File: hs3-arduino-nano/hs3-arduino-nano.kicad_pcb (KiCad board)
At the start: 2 copper layers, 17.8 x 43.2 mm, 40 parts, among them J1 PWR, J2 USB_B_Micro, J3 DBG, J4 I2C, J5 Sensors, J7 3V3, J8 GND, P3 CONN_01X01, P4 CONN_01X01, P5 CONN_01X01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

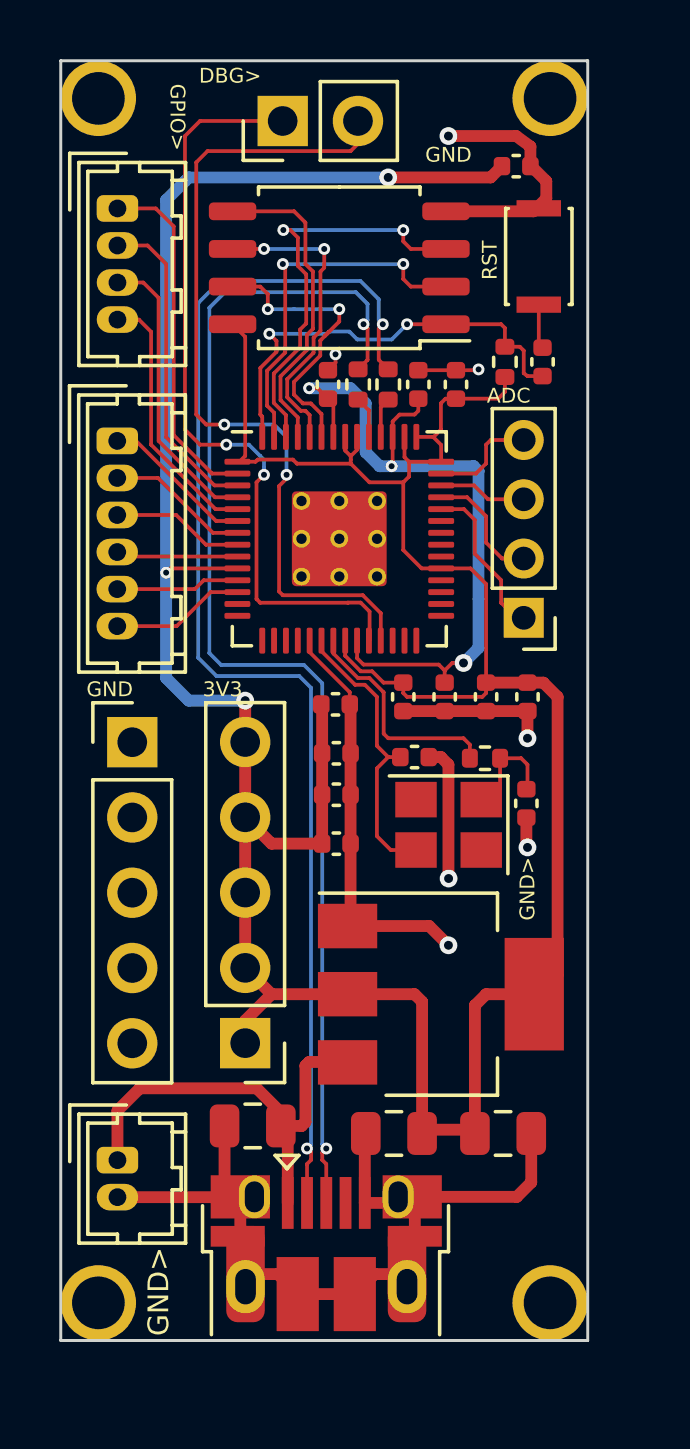
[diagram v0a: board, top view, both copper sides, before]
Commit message: Post-review place & route update pt. 1
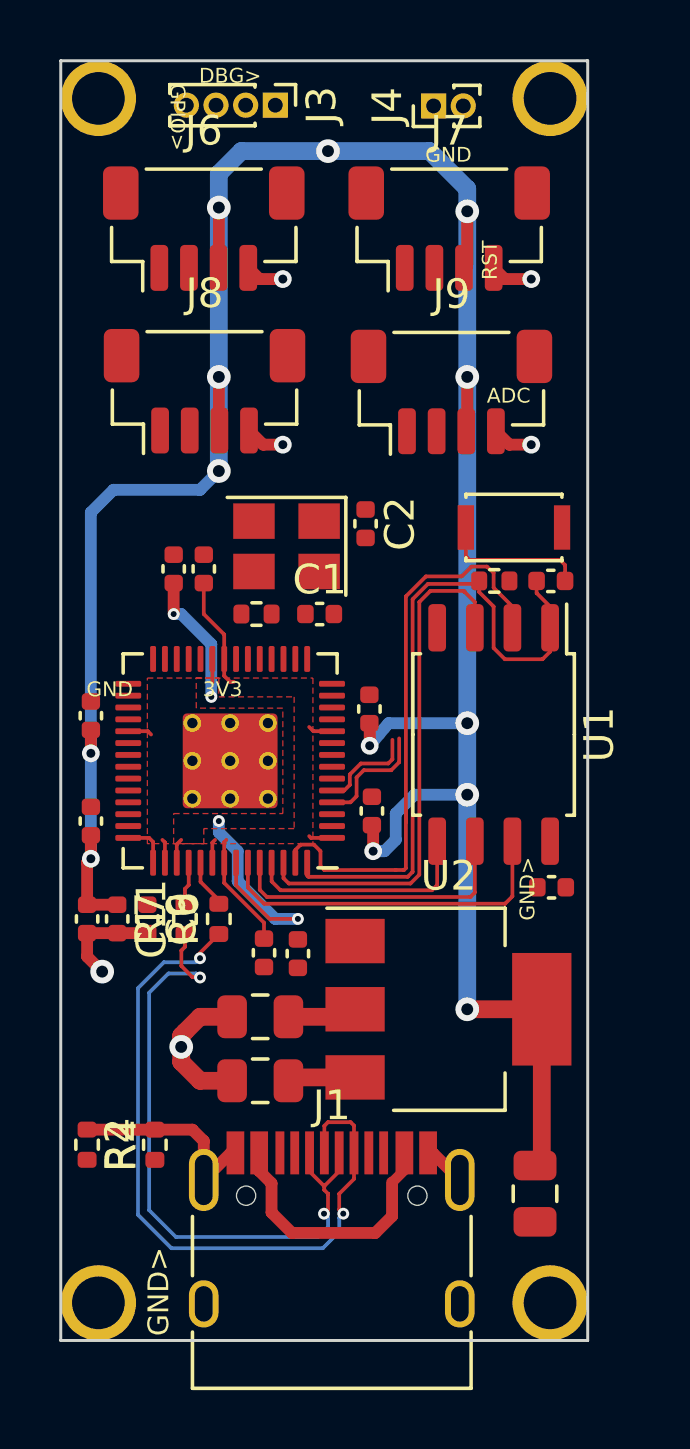
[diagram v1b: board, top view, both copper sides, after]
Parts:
- removed ADC: Conn_01x04, Connector_PinHeader_2.00mm:PinHeader_1x04_P2.00mm_Vertical
- removed J2: USB_B_Micro, RP2040:USB_Micro-B_Amphenol_10103594-0001LF_Horizontal_modified
- removed J5: Sensors, Connector_Hirose:Hirose_DF13-06P-1.25DSA_1x06_P1.25mm_Vertical
- added J6: CONN_01x04, Connector_JST:JST_SH_BM04B-SRSS-TB_1x04-1MP_P1.00mm_Vertical, F.Cu at (143.0, 73.1)
- added J9: CONN_01x04, Connector_JST:JST_SH_BM04B-SRSS-TB_1x04-1MP_P1.00mm_Vertical, F.Cu at (151.4, 78.6)
- added R6: 27, Resistor_SMD:R_0402_1005Metric, F.Cu at (143.5, 96.4)
- added R7: 27, Resistor_SMD:R_0402_1005Metric, F.Cu at (142.4, 96.4)
- J1: value PWR -> USB_C_Receptacle_USB2.0; footprint Connector_Hirose:Hirose_DF13-02P-1.25DSA_1x02_P1.25mm_Vertical -> Connector_USB:USB_C_Receptacle_HRO_TYPE-C-31-M-12
- J3: footprint Connector_PinHeader_2.54mm:PinHeader_1x02_P2.54mm_Vertical -> Connector_PinHeader_1.00mm:PinHeader_1x04_P1.00mm_Vertical
- J4: value I2C -> LED; footprint Connector_Hirose:Hirose_DF13-04P-1.25DSA_1x04_P1.25mm_Vertical -> Connector_PinHeader_1.00mm:PinHeader_1x02_P1.00mm_Vertical
- J7: value 3V3 -> CONN_01x04; footprint Connector_PinHeader_2.54mm:PinHeader_1x05_P2.54mm_Vertical -> Connector_JST:JST_SH_BM04B-SRSS-TB_1x04-1MP_P1.00mm_Vertical
- J8: value GND -> CONN_01x04; footprint Connector_PinHeader_2.54mm:PinHeader_1x05_P2.54mm_Vertical -> Connector_JST:JST_SH_BM04B-SRSS-TB_1x04-1MP_P1.00mm_Vertical
- R2: value 1k -> 5.1k
- R4: value 27 -> 5.1k
- R5: value 27 -> 1k
- U1: value NCP1117-3.3_SOT223 -> W25Q128JVS; footprint Package_TO_SOT_SMD:SOT-223-3_TabPin2 -> Package_SO:SOIC-8_5.23x5.23mm_P1.27mm
- U2: value W25Q128JVS -> NCP1117-3.3_SOT223; footprint Package_SO:SOIC-8_5.23x5.23mm_P1.27mm -> Package_TO_SOT_SMD:SOT-223-3_TabPin2
- moved J7 28.3 mm to (151.3, 73.1), turned to 0 degrees
- moved R4 27.2 mm to (139.1, 104.0)
- moved U2 25.3 mm to (151.3, 99.4), turned to 0 degrees
- moved C4 24.4 mm to (154.7, 95.3), turned to 180 degrees
- moved C11 21.4 mm to (140.1, 96.4), turned to -90 degrees
- moved C7 19.6 mm to (146.2, 97.6), turned to -90 degrees
- moved C9 19.0 mm to (141.1, 96.4), turned to -90 degrees
- moved R2 17.2 mm to (141.4, 104.0), turned to 90 degrees
- moved C17 15.4 mm to (139.1, 96.4)
- moved C16 12.4 mm to (145.0, 97.5)
- moved J8 12.1 mm to (143.0, 78.6)
- moved J4 11.2 mm to (150.8, 69.0), turned to 90 degrees
- moved C2 10.9 mm to (148.5, 83.1)
- moved XTAL1 10.9 mm to (145.8, 83.8)
- moved C13 10.3 mm to (143.0, 84.6), turned to 90 degrees
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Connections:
- J3 pad 1: /SWCLK -> +3V3
- J3 pad 2: /SWD -> /SWCLK
- J4 pad 1: /GPIO0 -> /GPIO2
- J4 pad 2: /GPIO1 -> /GPIO3
- J7 pad 1: +3V3 -> /GPIO17
- J7 pad 2: +3V3 -> /GPIO16
- J7 pad 4: +3V3 -> GND
- J8 pad 1: GND -> /GPIO17
- J8 pad 2: GND -> /GPIO16
- J8 pad 3: GND -> +3V3
- R2 pad 1: /XOUT -> Net-(J1-PadA5)
- R2 pad 2: Net-(C2-Pad1) -> GND
- R4 pad 1: /USB_D+ -> GND
- R4 pad 2: Net-(R4-Pad2) -> Net-(J1-PadB5)
- R5 pad 1: /USB_D- -> /XOUT
- R5 pad 2: Net-(R5-Pad2) -> Net-(C2-Pad1)
- U1 pad 1: GND -> /QSPI_SS
- U1 pad 2: +3V3 -> /QSPI_SD1
- U1 pad 3: VBUS -> /QSPI_SD2
- U2 pad 1: /QSPI_SS -> GND
- U2 pad 2: /QSPI_SD1 -> +3V3
- U2 pad 3: /QSPI_SD2 -> VBUS
- U3 pad 46: Net-(R5-Pad2) -> Net-(R7-Pad2)
- U3 pad 47: Net-(R4-Pad2) -> Net-(R6-Pad2)
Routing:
- net GND: track 61.5 -> 22.3 mm, vias 7 -> 6
- net /SWD: track 28.3 -> 0.00 mm, vias 2 -> 0
- net /SWCLK: track 26.3 -> 0.00 mm, vias 2 -> 0
- net /USB_D-: track 43.0 -> 20.8 mm
- net /USB_D+: track 41.8 -> 24.8 mm
- net /GPIO0: track 11.9 -> 0.00 mm
- net +3V3: track 120.4 -> 109.0 mm, vias 3 -> 13
- net /GPIO1: track 10.8 -> 0.00 mm
- net +1V1: track 24.6 -> 14.3 mm, vias 3 -> 4
- net /XIN: track 9.80 -> 0.00 mm
- net /QSPI_SS: track 14.9 -> 23.0 mm, vias 2 -> 0
- net /QSPI_SD1: track 12.3 -> 20.0 mm, vias 2 -> 0
- net /XOUT: track 7.59 -> 0.00 mm
- net /GPIO26_ADC0: track 6.29 -> 0.00 mm
- net /GPIO2: track 9.88 -> 4.00 mm
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- added copper zone on F.Cu, net +1V1
- added copper zone on F.Cu, net +3V3

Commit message: Post-review place & route update pt. 2
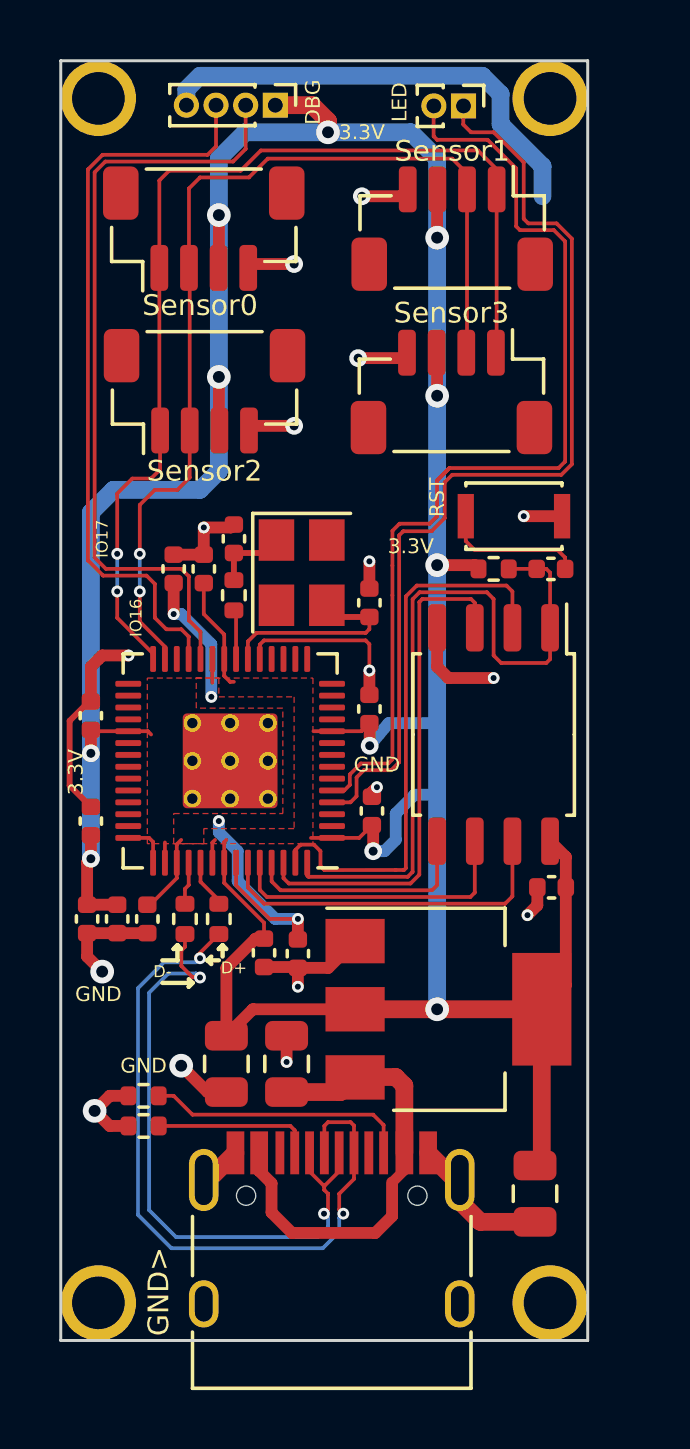
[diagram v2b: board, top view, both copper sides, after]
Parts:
- moved G2 12.8 mm to (147.1, 84.6)
- moved C2 4.47 mm to (144.0, 83.6), turned to 90 degrees
- moved R4 2.52 mm to (141.0, 102.4), turned to 0 degrees
- moved C6 1.96 mm to (143.8, 101.3), turned to -90 degrees
- moved C1 1.72 mm to (148.6, 85.7), turned to 90 degrees
- moved C3 1.06 mm to (145.8, 101.3), turned to 90 degrees
- moved XTAL1 1.02 mm to (146.3, 84.7), turned to -90 degrees
- moved J4 1.01 mm to (151.8, 69.0), turned to -90 degrees
- moved R5 0.99 mm to (144.0, 85.5), turned to 90 degrees
- moved R2 0.74 mm to (141.0, 103.4), turned to 180 degrees
- moved R3 0.41 mm to (152.8, 84.6), turned to 0 degrees
- moved R1 0.41 mm to (154.7, 84.6)
- moved SW1 0.38 mm to (153.5, 82.8)
- moved Sensor1 0.10 mm to (151.4, 73.1), turned to 180 degrees
- turned Sensor3 to 180 degrees
- renumbered J7 to Sensor1, J8 to Sensor2, J9 to Sensor3
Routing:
- net GND: track 22.3 -> 64.6 mm, vias 6 -> 17
- net /GPIO17: track 0.00 -> 35.9 mm, vias 0 -> 2
- net /GPIO16: track 0.00 -> 33.4 mm, vias 0 -> 2
- net /GPIO3: track 3.34 -> 33.9 mm
- net /GPIO2: track 4.00 -> 33.0 mm
- net /SWCLK: track 0.00 -> 26.3 mm
- net /SWD: track 0.00 -> 25.1 mm
- net +3V3: track 109.0 -> 130.1 mm, vias 13 -> 11
- net Net-(J1-PadB5): track 0.00 -> 8.94 mm
- net /XIN: track 0.00 -> 6.87 mm
- net Net-(J1-PadA5): track 0.00 -> 5.41 mm
- net VBUS: track 11.6 -> 15.7 mm
- net +1V1: track 14.3 -> 16.9 mm
- net Net-(C2-Pad1): track 0.00 -> 2.53 mm
- net /XOUT: track 0.00 -> 1.67 mm
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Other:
- board text added: "3.3V"
- board text added: "D+"
- board text added: "D-"
- board text added: "DBG"
- board text added: "IO16"
- board text added: "IO17"
- board text added: "LED"
- board text removed: "3V3"
- board text removed: "ADC"
- board text removed: "ADC0"
- board text removed: "ADC1"
- board text removed: "ADC2"
- board text removed: "ADC3"
- board text removed: "DBG>"
- board text removed: "GPIO>"
- board text removed: "IO0"
- board text removed: "IO1"
- board text removed: "IO2"
- board text removed: "IO3"
- board text removed: "IO4"
- board text removed: "IO5"
- board text removed: "IO6"
- board text removed: "IO7"
- board text removed: "IO8"
- board text removed: "IO9"

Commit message: Shortening traces around 3.3V pins
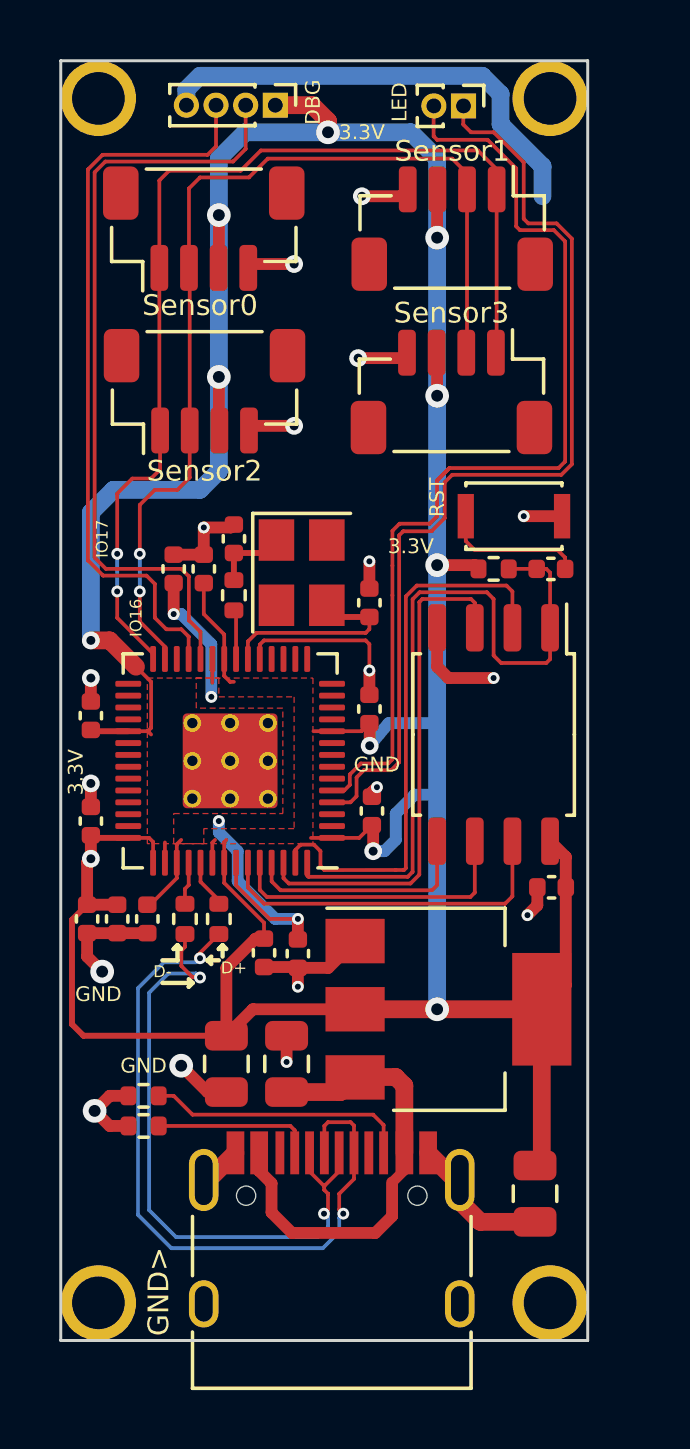
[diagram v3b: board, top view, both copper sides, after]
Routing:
- net +3V3: track 130.1 -> 137.2 mm
- net GND: track 64.6 -> 59.4 mm, vias 17 -> 18

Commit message: Minor cleanup in PCB, adding part numbers to BOM
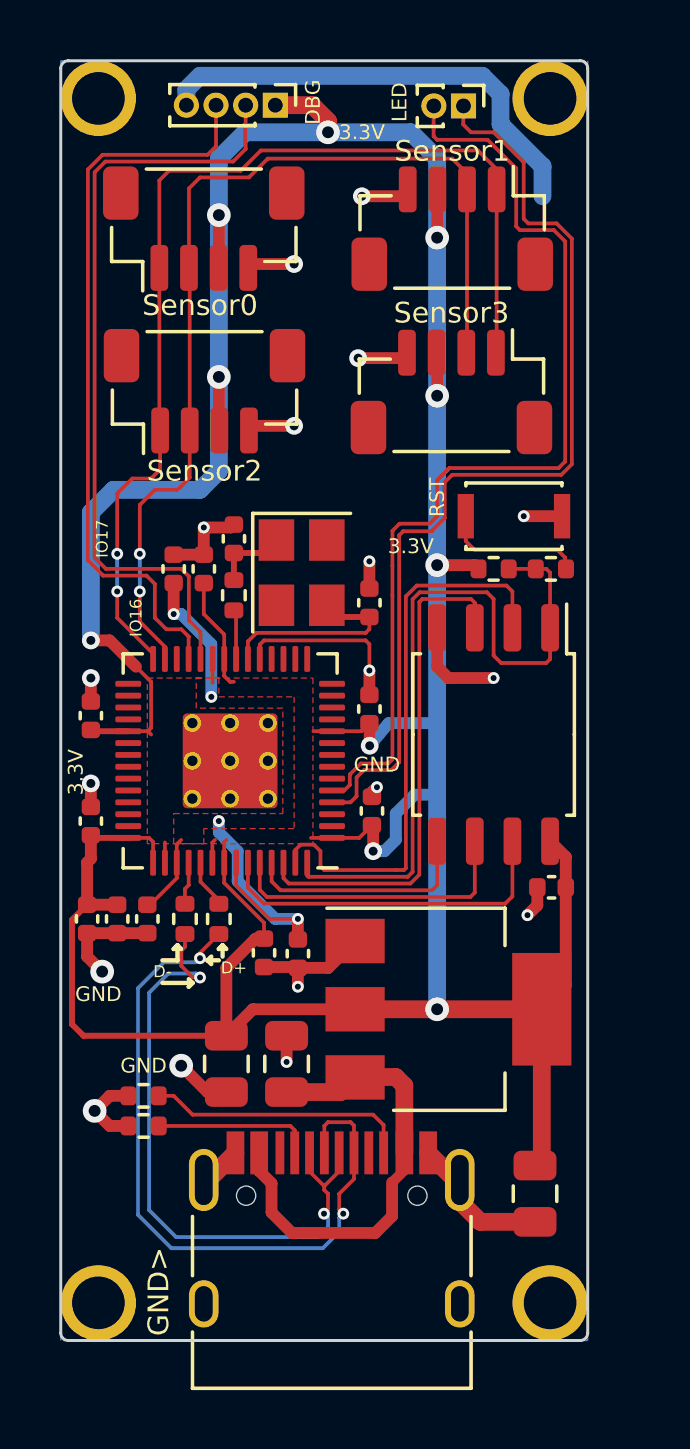
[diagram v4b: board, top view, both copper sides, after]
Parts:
- R1: footprint Capacitor_SMD:C_0402_1005Metric -> Resistor_SMD:R_0402_1005Metric
- moved G2 3.79 mm to (144.7, 87.5)
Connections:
- net /GPIO2 renamed Net-(J4-Pad1)
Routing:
- net +3V3: vias 11 -> 10
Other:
- outline, holes or cut-outs redrawn
- board text added: "Cyberskakanka"
